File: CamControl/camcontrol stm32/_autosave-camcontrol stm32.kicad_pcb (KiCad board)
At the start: 4 copper layers, 15.9 x 33.8 mm, 54 parts, among them J1 Power 1, J2 Conn_01x04, J3 Power 1, J4 Power 1, J5 Conn_01x06, J6 Conn_01x02, J7 Power 1, Q1 AO3401A, U1 BGS12P2L6, U2 BALFHB-WL-02D3, U3 STM32WLE4CCUx, U4 DS8242, U5 TPS25970LRPWR, U6 TPS25970LRPWR, U7 INA2180, Y1 32MHz

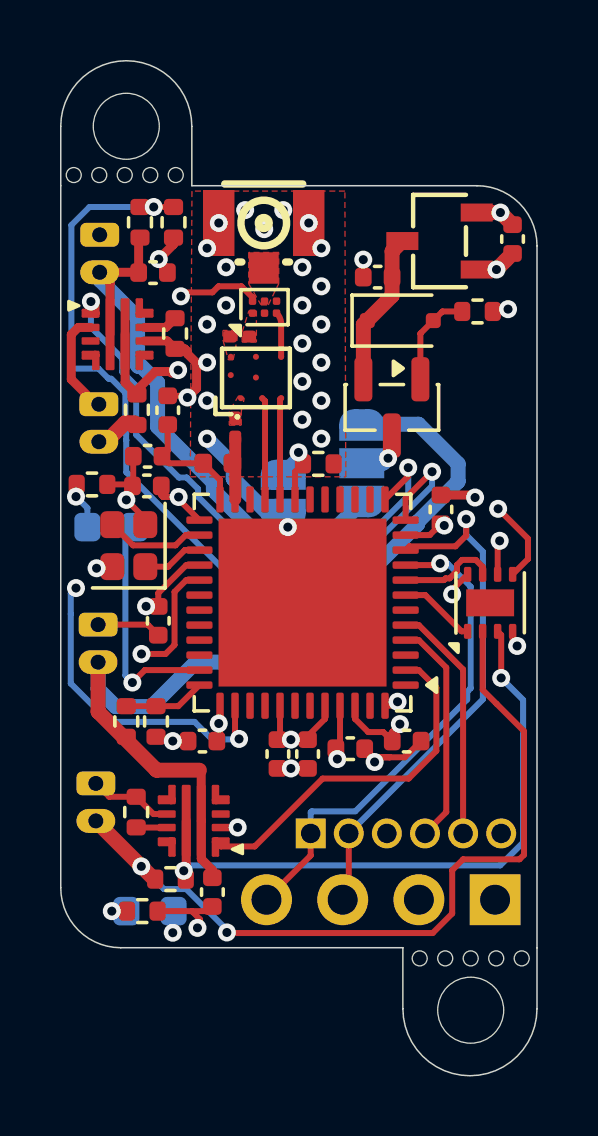
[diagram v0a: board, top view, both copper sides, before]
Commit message: rf rework and redrawing
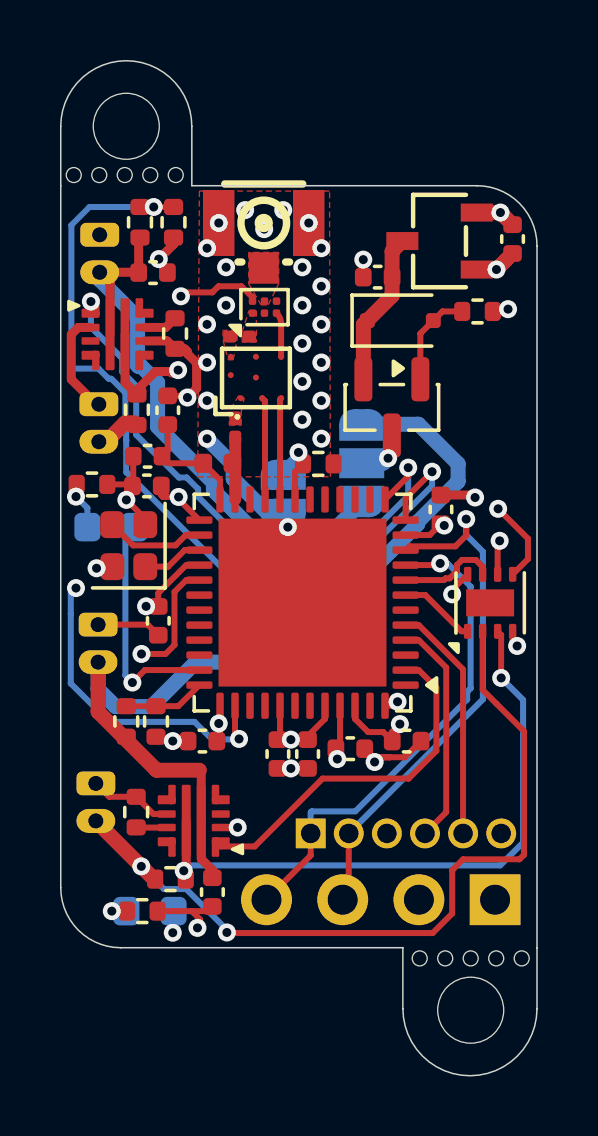
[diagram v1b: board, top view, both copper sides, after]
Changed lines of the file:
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@@
 		(polygon
 			(pts
-				(xy 168.4528 129.54) (xy 168.424702 120.015) (xy 163.327244 120.015) (xy 163.27105 129.54)
+				(xy 167.9412 129.54) (xy 167.913102 120.015) (xy 163.574044 120.015) (xy 163.51785 129.54)
 			)
 		)
